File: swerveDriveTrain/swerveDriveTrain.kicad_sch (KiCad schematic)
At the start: 0 parts

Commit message: worked on swerve drive train board
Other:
- added sheet InputOutputPorts (IO.kicad_sch)
- added sheet PowerManagement (PowerManagement.kicad_sch)
- added sheet Teensy (Teensy.kicad_sch)
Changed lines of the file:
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@@
 	(generator_version "8.0")
 	(paper "A4")
+	(sheet
+		(at 19.05 21.59)
+		(size 50.8 43.18)
+		(fields_autoplaced yes)
+		(stroke
+			(width 0.1524)
+			(type solid)
+		)
+		(fill
+			(color 0 0 0 0.0000)
+		)
+		(property "Sheetname" "Teensy"
+			(at 19.05 20.8784 0)
+			(effects
+				(font
+					(size 1.27 1.27)
+				)
+				(justify left bottom)
+			)
+		)
+		(property "Sheetfile" "Teensy.kicad_sch"
+			(at 19.05 65.3546 0)
+			(effects
+				(font
+					(size 1.27 1.27)
+				)
+				(justify left top)
+			)
+		)
+		(instances
+			(project "swerveDriveTrain"
+				(path "/ffff3ec3-318d-4aa9-9cdd-5e805c5c485a"
+					(page "2")
+				)
+			)
+		)
+	)
+	(sheet
+		(at 82.55 21.59)
+		(size 57.15 43.18)
+		(fields_autoplaced yes)
+		(stroke
+			(width 0.1524)
+			(type solid)
+		)
+		(fill
+			(color 0 0 0 0.0000)
+		)
+		(property "Sheetname" "PowerManagement"
+			(at 82.55 20.8784 0)
+			(effects
+				(font
+					(size 1.27 1.27)
+				)
+				(justify left bottom)
+			)
+		)
+		(property "Sheetfile" "PowerManagement.kicad_sch"
+			(at 82.55 65.3546 0)
+			(effects
+				(font
+					(size 1.27 1.27)
+				)
+				(justify left top)
+			)
+		)
+		(instances
+			(project "swerveDriveTrain"
+				(path "/ffff3ec3-318d-4aa9-9cdd-5e805c5c485a"
+					(page "3")
+				)
+			)
+		)
+	)
+	(sheet
+		(at 152.4 21.59)
+		(size 50.8 41.91)
+		(fields_autoplaced yes)
+		(stroke
+			(width 0.1524)
+			(type solid)
+		)
+		(fill
+			(color 0 0 0 0.0000)
+		)
+		(property "Sheetname" "InputOutputPorts"
+			(at 152.4 20.8784 0)
+			(effects
+				(font
+					(size 1.27 1.27)
+				)
+				(justify left bottom)
+			)
+		)
+		(property "Sheetfile" "IO.kicad_sch"
+			(at 152.4 64.0846 0)
+			(effects
+				(font
+					(size 1.27 1.27)
+				)
+				(justify left top)
+			)
+		)
+		(instances
+			(project "swerveDriveTrain"
+				(path "/ffff3ec3-318d-4aa9-9cdd-5e805c5c485a"
+					(page "5")
+				)
+			)
+		)
+	)
 	(sheet_instances
 		(path "/"

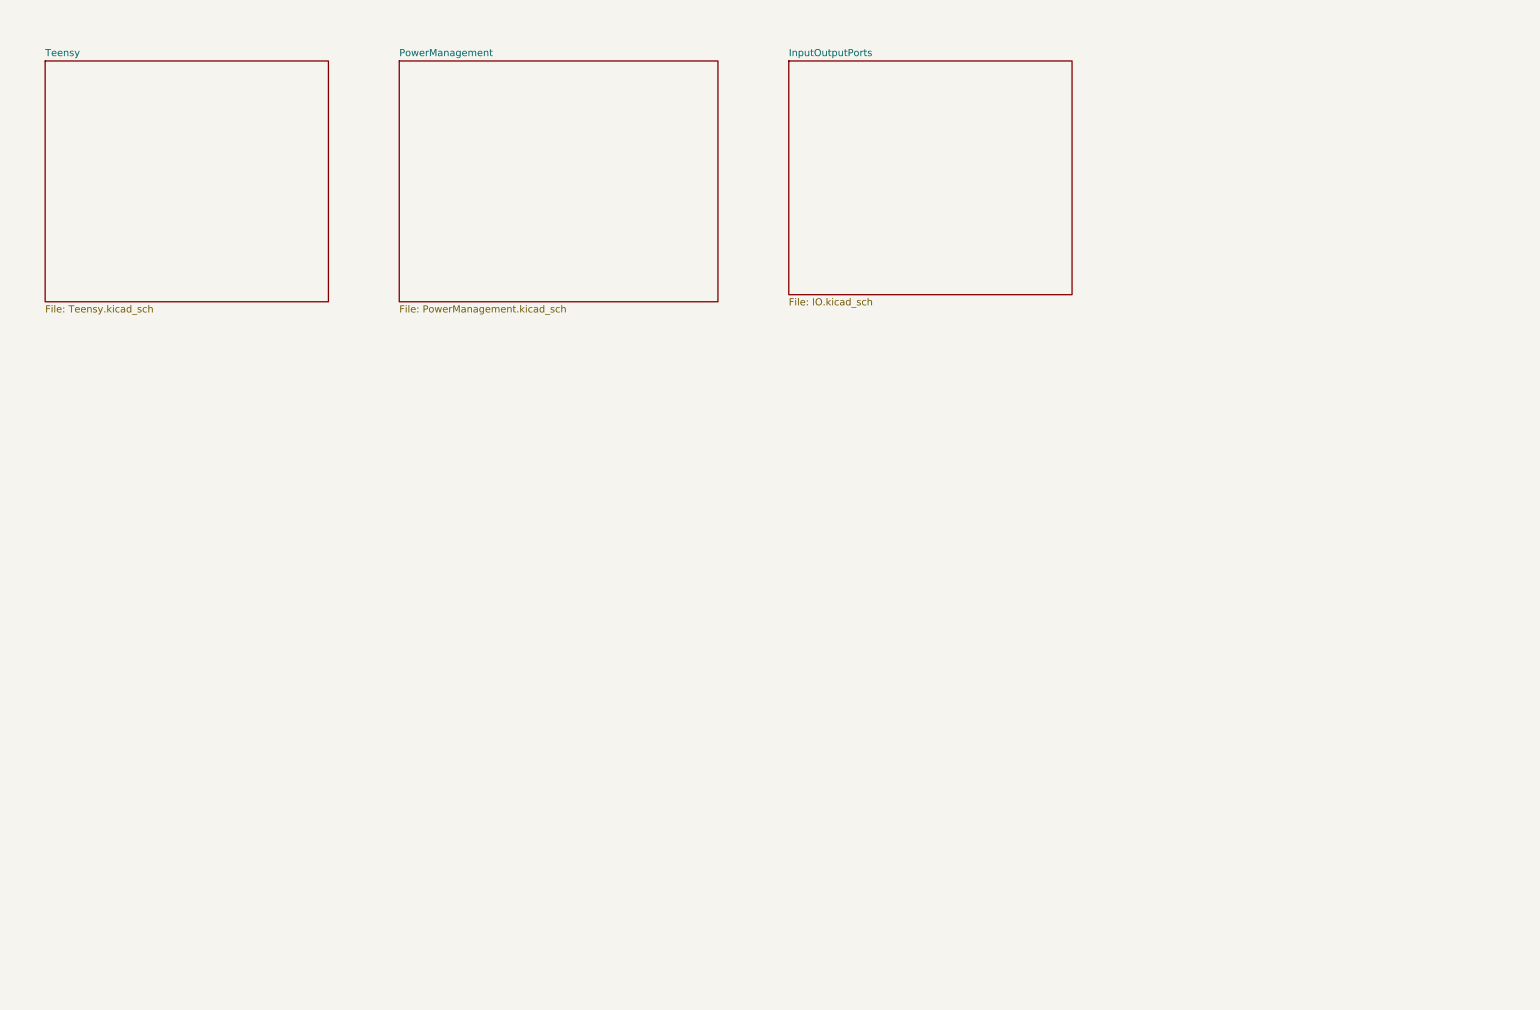
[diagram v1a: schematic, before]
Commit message: simplify schematic
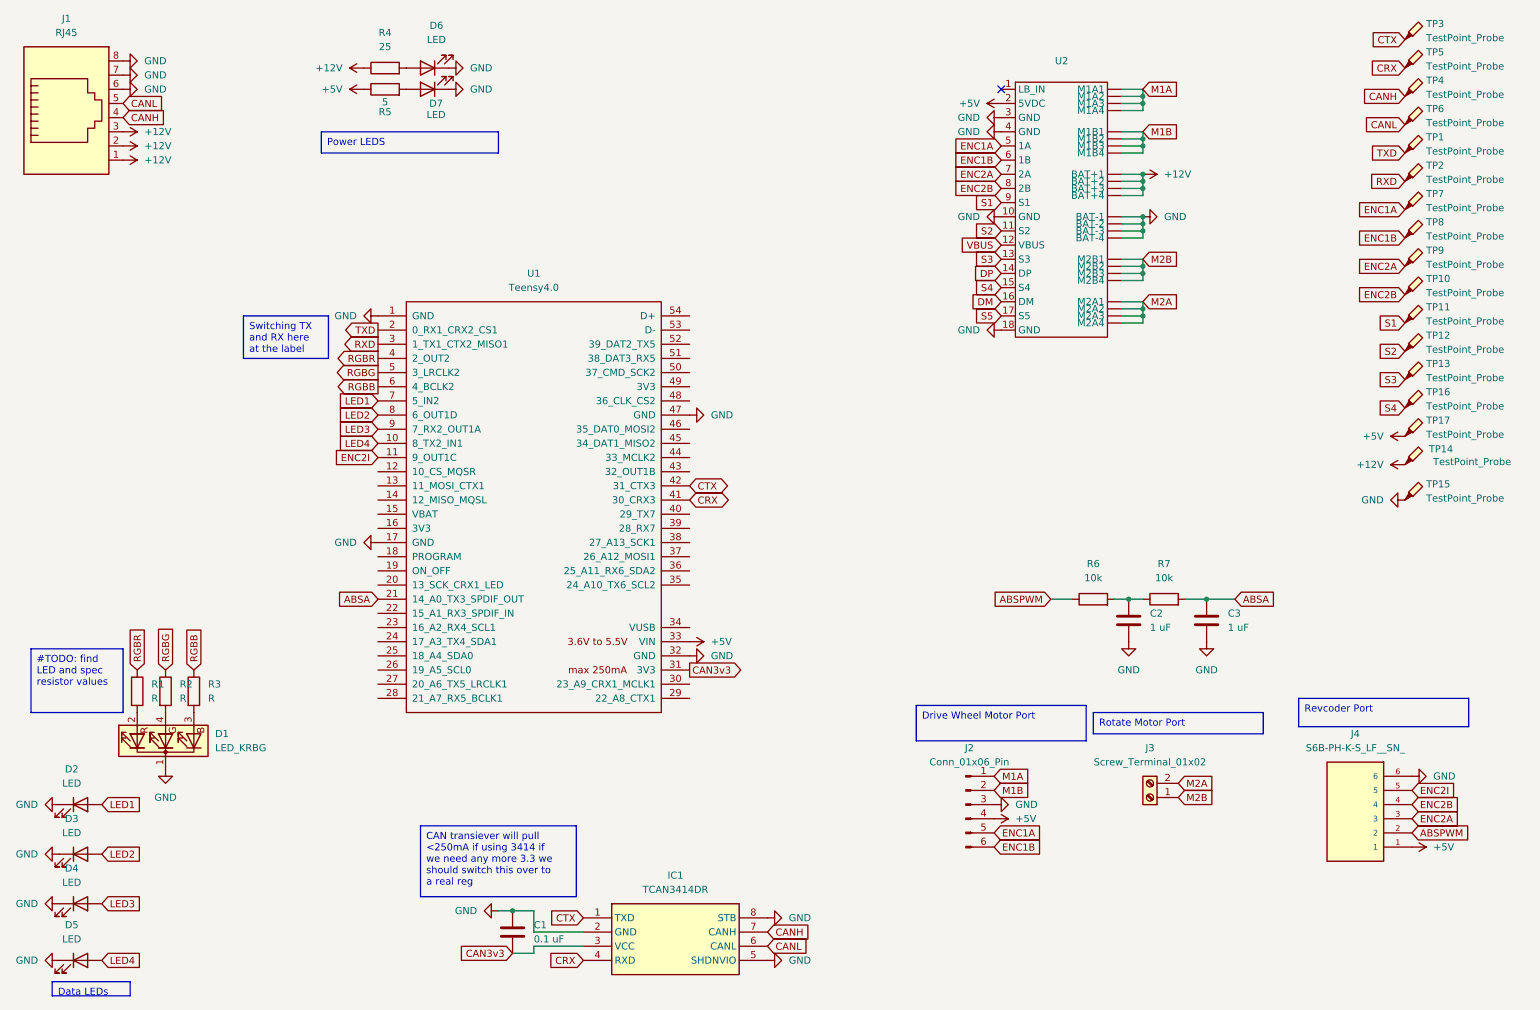
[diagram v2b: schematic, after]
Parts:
- added C1: 0.1 uF, symbol Device:C
- added C2, C3: 1 uF, symbol Device:C
- added D1: LED_KRBG, symbol Device:LED_KRBG
- added D2, D3, D4, D5, D6, D7: LED, symbol Device:LED
- added IC1: TCAN3414DR, SOIC127P600X175-8N, symbol TCAN3414DR:TCAN3414DR
- added J1: RJ45, symbol Connector:RJ45
- added J2: Conn_01x06_Pin, symbol Connector:Conn_01x06_Pin
- added J3: Screw_Terminal_01x02, symbol Connector:Screw_Terminal_01x02
- added J4: S6B-PH-K-S_LF__SN_, S6B-PH-K-S_LF__SN_:JST_S6B-PH-K-S_LF__SN_, symbol S6B-PH-K-S_LF__SN_:S6B-PH-K-S_LF__SN_
- added R1, R2, R3: R, symbol Device:R
- added R4: 25, symbol Device:R
- added R5: 5, symbol Device:R
- added R6, R7: 10k, symbol Device:R
- added TP1, TP10, TP11, TP12, TP13, TP14, TP15, TP16, TP17, TP2, TP3, TP4, TP5, TP6, TP7, TP8, TP9: TestPoint_Probe, symbol Connector:TestPoint_Probe
- added U1: Teensy4.0, symbol teensy:Teensy4.0
- added U2: ~, symbol roboclaw:Roboclaw
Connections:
- new net: D1.3 (BA), R3.2
- new net: D1.2 (RA), R1.2
- new net: D1.4 (GA), R2.2
- new net: C2.2, R6.2, R7.1
- new net: D7.2 (A), R5.2
- new net: D6.2 (A), R4.2
- new net +12V: J1.1, J1.2, J1.3, R4.1, TP14.1, U2. (M2B4)
- new net +5V: J2.4 (Pin_4), J4.1, R5.1, TP17.1, U1.33 (VIN), U2.2 (5VDC)
- new net ABSA: C3.1, R7.2, U1.21 (14_A0_TX3_SPDIF_OUT)
- new net ABSPWM: J4.2, R6.1
- new net CAN3v3: C1.2, IC1.3 (VCC), U1.31 (3V3)
- new net CANH: IC1.7 (CANH), J1.4, TP4.1
- new net CANL: IC1.6 (CANL), J1.5, TP6.1
- new net CRX: IC1.4 (RXD), TP5.1, U1.41 (30_CRX3)
- new net CTX: IC1.1 (TXD), TP3.1, U1.42 (31_CTX3)
- new net DM: U2.16 (DM)
- new net DP: U2.14 (DP)
- new net ENC1A: J2.5 (Pin_5), TP7.1, U2.5 (1A)
- new net ENC1B: J2.6 (Pin_6), TP8.1, U2.6 (1B)
- new net ENC2A: J4.3, TP9.1, U2.7 (2A)
- new net ENC2B: J4.4, TP10.1, U2.8 (2B)
- new net ENC2I: J4.5, U1.11 (9_OUT1C)
- new net GND: C1.1, C2.1, C3.2, D1.1 (K), D2.1 (K), D3.1 (K), D4.1 (K), D5.1 (K), D6.1 (K), D7.1 (K), IC1.2 (GND), IC1.5 (SHDNVIO), IC1.8 (STB), J1.6, J1.7, J1.8, J2.3 (Pin_3), J4.6, TP15.1, U1.1 (GND), U1.17 (GND), U1.32 (GND), U1.47 (GND), U2. (M2B4), U2.10 (GND), U2.18 (GND), U2.3 (GND), U2.4 (GND)
- new net LED1: D2.2 (A), U1.7 (5_IN2)
- new net LED2: D3.2 (A), U1.8 (6_OUT1D)
- new net LED3: D4.2 (A), U1.9 (7_RX2_OUT1A)
- new net LED4: D5.2 (A), U1.10 (8_TX2_IN1)
- new net M1A: J2.1 (Pin_1), U2. (M2B4)
- new net M1B: J2.2 (Pin_2), U2. (M2B4)
- new net M2A: J3.2 (Pin_2), U2. (M2B4)
- new net M2B: J3.1 (Pin_1), U2. (M2B4)
- new net RGBB: R3.1, U1.6 (4_BCLK2)
- new net RGBG: R2.1, U1.5 (3_LRCLK2)
- new net RGBR: R1.1, U1.4 (2_OUT2)
- new net RXD: TP2.1, U1.3 (1_TX1_CTX2_MISO1)
- new net S1: TP11.1, U2.9 (S1)
- new net S2: TP12.1, U2.11 (S2)
- new net S3: TP13.1, U2.13 (S3)
- new net S4: TP16.1, U2.15 (S4)
- new net S5: U2.17 (S5)
- new net TXD: TP1.1, U1.2 (0_RX1_CRX2_CS1)
- new net VBUS: U2.12 (VBUS)
- no-connect marks 0 -> 1
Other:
- removed sheet InputOutputPorts
- removed sheet PowerManagement
- removed sheet Teensy

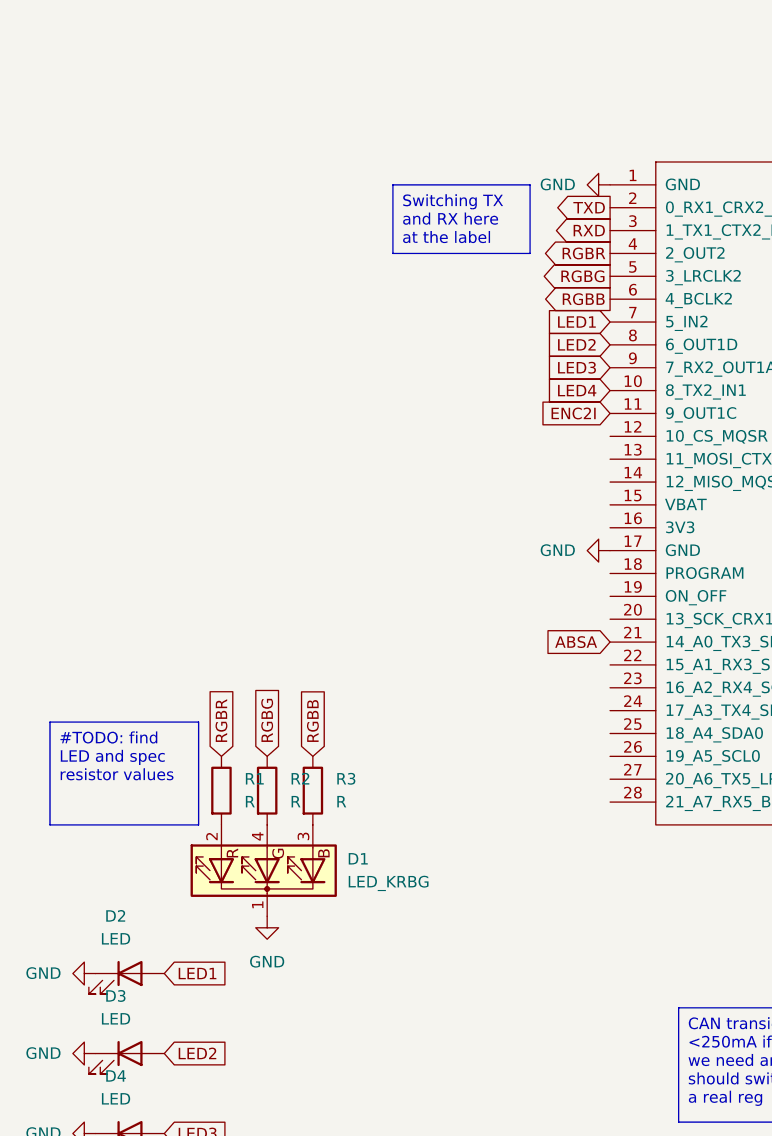
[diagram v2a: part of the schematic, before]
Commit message: add rgb led
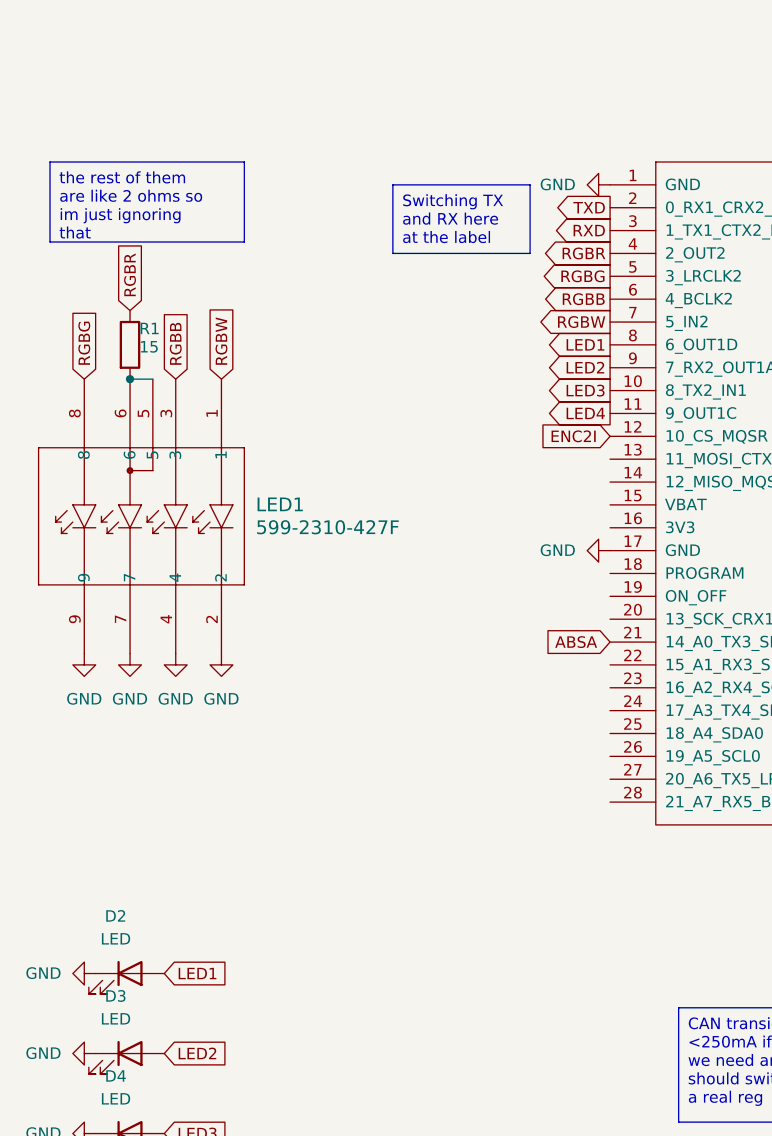
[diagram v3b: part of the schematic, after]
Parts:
- removed D1: LED_KRBG, symbol Device:LED_KRBG
- removed R2, R3: R, symbol Device:R
- added LED1: 599-2310-427F, 599-2310_DIA, symbol 2024-05-06_00-08-00:599-2310-427F
- R1: value R -> 15
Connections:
- net ENC2I: now also U1.12 (10_CS_MQSR); no longer U1.11 (9_OUT1C)
- net GND: now also LED1.2, LED1.4, LED1.7, LED1.9
- net LED1: now also U1.8 (6_OUT1D); no longer U1.7 (5_IN2)
- net LED2: now also U1.9 (7_RX2_OUT1A); no longer U1.8 (6_OUT1D)
- net LED3: now also U1.10 (8_TX2_IN1); no longer U1.9 (7_RX2_OUT1A)
- net LED4: now also U1.11 (9_OUT1C); no longer U1.10 (8_TX2_IN1)
- net RGBB: now also LED1.3
- net RGBG: now also LED1.8
- net at R1.2: now also LED1.5, LED1.6
- new net RGBW: LED1.1, U1.7 (5_IN2)

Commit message: added footprints to everything + other updates
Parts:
- added C4: 0.1 uF, Capacitor_SMD:C_0805_2012Metric, symbol Device:C
- added P1: USB_C_Plug_USB2.0, Connector_USB:USB_C_Receptacle_GCT_USB4085, symbol Connector:USB_C_Plug_USB2.0
- C1: renamed from C2; footprint (none) -> Capacitor_SMD:C_0805_2012Metric
- C2: renamed from C3; footprint (none) -> Capacitor_SMD:C_0805_2012Metric
- C3: renamed from C1; footprint (none) -> Capacitor_SMD:C_0805_2012Metric
- D1: renamed from D6; footprint (none) -> GreenLED:LED_CREE_MLXXXX
- D2: renamed from D7; footprint (none) -> GreenLED:LED_CREE_MLXXXX
- D3: renamed from D2; footprint (none) -> GreenLED:LED_CREE_MLXXXX
- D4: renamed from D3; footprint (none) -> GreenLED:LED_CREE_MLXXXX
- D5: renamed from D4; footprint (none) -> GreenLED:LED_CREE_MLXXXX
- D6: renamed from D5; footprint (none) -> GreenLED:LED_CREE_MLXXXX
- IC1: footprint SOIC127P600X175-8N -> footprints:SOIC127P600X175-8N
- J1: footprint (none) -> Connector_RJ:RJ45_Amphenol_54602-x08_Horizontal
- J2: renamed from J3; footprint (none) -> footprints:PHOENIX_1935161
- J3: renamed from J2; footprint (none) -> Connector_PinHeader_2.54mm:PinHeader_1x06_P2.54mm_Horizontal
- J4: footprint S6B-PH-K-S_LF__SN_:JST_S6B-PH-K-S_LF__SN_ -> footprints:JST_S6B-PH-K-S_LF__SN_
- LED1: footprint 599-2310_DIA -> footprints:599-2310_DIA
- R1: renamed from R4; footprint (none) -> Resistor_SMD:R_0805_2012Metric
- R2: renamed from R5; footprint (none) -> Resistor_SMD:R_0805_2012Metric
- R3: renamed from R1; footprint (none) -> Resistor_SMD:R_0805_2012Metric
- R4: renamed from R6; footprint (none) -> Resistor_SMD:R_0805_2012Metric
- R5: renamed from R7; footprint (none) -> Resistor_SMD:R_0805_2012Metric
- TP1: renamed from TP3; footprint (none) -> TestPoint:TestPoint_Pad_D4.0mm
- TP10, TP11, TP12, TP13, TP7, TP8, TP9: footprint (none) -> TestPoint:TestPoint_Pad_D4.0mm
- TP14: renamed from TP16; footprint (none) -> TestPoint:TestPoint_Pad_D4.0mm
- TP15: renamed from TP17; footprint (none) -> TestPoint:TestPoint_Pad_D4.0mm
- TP16: renamed from TP14; footprint (none) -> TestPoint:TestPoint_Pad_D4.0mm
- TP17: renamed from TP15; footprint (none) -> TestPoint:TestPoint_Pad_D4.0mm
- TP2: renamed from TP5; footprint (none) -> TestPoint:TestPoint_Pad_D4.0mm
- TP3: renamed from TP4; footprint (none) -> TestPoint:TestPoint_Pad_D4.0mm
- TP4: renamed from TP6; footprint (none) -> TestPoint:TestPoint_Pad_D4.0mm
- TP5: renamed from TP1; footprint (none) -> TestPoint:TestPoint_Pad_D4.0mm
- TP6: renamed from TP2; footprint (none) -> TestPoint:TestPoint_Pad_D4.0mm
- U1: renamed from U2; footprint (none) -> Custom:roboclaw
- U2: renamed from U1; footprint (none) -> teensy:Teensy40_SMT
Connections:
- net +12V: now also U1.27 (BAT+1), U1.28 (BAT+2), U1.29 (BAT+3), U1.30 (BAT+4); no longer U1. (M2B4)
- net +5V: now also C4.1
- net DM: now also P1.A6 (D+)
- net DP: now also P1.A7 (D-)
- net GND: now also U1.31 (BAT-1), U1.32 (BAT-2), U1.33 (BAT-3), U1.34 (BAT-4), C4.2, P1.A1 (GND), P1.A12 (GND), P1.B1 (GND), P1.B12 (GND), P1.S1 (SHIELD); no longer U1. (M2B4)
- net M1A: now also U1.19 (M1A1), U1.20 (M1A2), U1.21 (M1A3), U1.22 (M1A4); no longer U1. (M2B4)
- net M1B: now also U1.23 (M1B1), U1.24 (M1B2), U1.25 (M1B3), U1.26 (M1B4); no longer U1. (M2B4)
- net M2A: now also U1.39 (M2A1), U1.40 (M2A2), U1.41 (M2A3), U1.42 (M2A4); no longer U1. (M2B4)
- net M2B: now also U1.35 (M2B1), U1.36 (M2B2), U1.37 (M2B3), U1.38 (M2B4); no longer U1. (M2B4)
- net VBUS: now also P1.A4 (VBUS), P1.A9 (VBUS), P1.B4 (VBUS), P1.B9 (VBUS)
- no-connect marks 1 -> 3
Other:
- note added: "Roboclaw"
- moved on the sheet: C1, C2, J3, R4, R5
